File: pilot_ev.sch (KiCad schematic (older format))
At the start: 9 parts, among them Q201 AO3400A

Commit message: Add files via upload
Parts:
- removed TP201: TP_EV_PILOT, symbol Connector:TestPoint_Flag
- removed TP202: TP_EV_PILOT_ADC, symbol Connector:TestPoint_Flag
- added R206, R207: 200, Resistor_SMD:R_0402_1005Metric, symbol Device:R_Small_US
- added R208: 100, Resistor_SMD:R_0402_1005Metric, symbol Device:R_Small_US
- D201: footprint (none) -> Diode_SMD:D_SOD-123F
- Q201: footprint (none) -> Package_TO_SOT_SMD:SOT-23
- R201: value 2k74 -> 2k7; footprint (none) -> Resistor_SMD:R_0603_1608Metric
- R202, R204, R205: footprint (none) -> Resistor_SMD:R_0402_1005Metric
- R203: value 1k3 -> 1k2; footprint (none) -> Resistor_SMD:R_0402_1005Metric
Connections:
- wire segments 18 -> 22
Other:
- note added: "Total: 1k3"
- note added: "Total: 2k74"
- moved on the sheet: R203
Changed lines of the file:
@@
 U 1 1 5EEF9EDE
 P 3050 2600
-F 0 "R201" H 2982 2554 50  0000 R CNN
-F 1 "2k74" H 2982 2645 50  0000 R CNN
-F 2 "" H 3050 2600 50  0001 C CNN
+F 0 "R201" H 3300 2550 50  0000 R CNN
+F 1 "2k7" H 3300 2650 50  0000 R CNN
+F 2 "Resistor_SMD:R_0603_1608Metric" H 3050 2600 50  0001 C CNN
 F 3 "~" H 3050 2600 50  0001 C CNN
 	1    3050 2600
@@
 L Device:R_Small_US R203
 U 1 1 5EEFAC97
-P 3500 2600
-F 0 "R203" H 3432 2554 50  0000 R CNN
-F 1 "1k3" H 3432 2645 50  0000 R CNN
-F 2 "" H 3500 2600 50  0001 C CNN
-F 3 "~" H 3500 2600 50  0001 C CNN
-	1    3500 2600
+P 3500 2450
+F 0 "R203" H 3432 2404 50  0000 R CNN
+F 1 "1k2" H 3432 2495 50  0000 R CNN
+F 2 "Resistor_SMD:R_0402_1005Metric" H 3500 2450 50  0001 C CNN
+F 3 "~" H 3500 2450 50  0001 C CNN
+	1    3500 2450
 	-1   0    0    1
 $EndComp
@@
 F 0 "D201" H 2800 2093 50  0000 C CNN
 F 1 "SM4007PL" H 2800 2184 50  0000 C CNN
-F 2 "" V 2800 2300 50  0001 C CNN
+F 2 "Diode_SMD:D_SOD-123F" V 2800 2300 50  0001 C CNN
 F 3 "~" V 2800 2300 50  0001 C CNN
 	1    2800 2300
@@
 Wire Wire Line
 	2900 2300 3050 2300
-Wire Wire Line
-	3050 2300 3500 2300
-Wire Wire Line
-	3500 2300 3500 2500
 Connection ~ 3050 2300
 Wire Wire Line
@@
 F 0 "Q201" H 3605 3146 50  0000 L CNN
 F 1 "AO3400A" H 3605 3055 50  0000 L CNN
-F 2 "" H 3600 3200 50  0001 C CNN
+F 2 "Package_TO_SOT_SMD:SOT-23" H 3600 3200 50  0001 C CNN
 F 3 "~" H 3400 3100 50  0001 C CNN
 	1    3400 3100
-	1    0    0    -1
-$EndComp
-Wire Wire Line
-	3500 2900 3500 2700
-$Comp
-L power:GND #PWR0201
-U 1 1 5EEFDC0F
-P 3050 2750
-F 0 "#PWR0201" H 3050 2500 50  0001 C CNN
-F 1 "GND" H 3055 2577 50  0000 C CNN
-F 2 "" H 3050 2750 50  0001 C CNN
-F 3 "" H 3050 2750 50  0001 C CNN
-	1    3050 2750
 	1    0    0    -1
 $EndComp
@@
 F 0 "R204" H 4182 2554 50  0000 R CNN
 F 1 "47k" H 4182 2645 50  0000 R CNN
-F 2 "" H 4250 2600 50  0001 C CNN
+F 2 "Resistor_SMD:R_0402_1005Metric" H 4250 2600 50  0001 C CNN
 F 3 "~" H 4250 2600 50  0001 C CNN
 	1    4250 2600
@@
 F 0 "R205" H 4182 3054 50  0000 R CNN
 F 1 "18k" H 4182 3145 50  0000 R CNN
-F 2 "" H 4250 3100 50  0001 C CNN
+F 2 "Resistor_SMD:R_0402_1005Metric" H 4250 3100 50  0001 C CNN
 F 3 "~" H 4250 3100 50  0001 C CNN
 	1    4250 3100
@@
 $EndComp
 Wire Wire Line
-	3500 2300 4250 2300
-Wire Wire Line
 	4250 2300 4250 2500
-Connection ~ 3500 2300
 Wire Wire Line
 	4250 3000 4250 2850
@@
 F 0 "R202" H 2982 3204 50  0000 R CNN
 F 1 "10k" H 2982 3295 50  0000 R CNN
-F 2 "" H 3050 3250 50  0001 C CNN
+F 2 "Resistor_SMD:R_0402_1005Metric" H 3050 3250 50  0001 C CNN
 F 3 "~" H 3050 3250 50  0001 C CNN
 	1    3050 3250
@@
 $EndComp
 $Comp
-L Connector:TestPoint_Flag TP201
-U 1 1 5EF8CC23
-P 4250 2300
-F 0 "TP201" H 4510 2394 50  0000 L CNN
-F 1 "TP_EV_PILOT" H 4510 2303 50  0000 L CNN
-F 2 "" H 4450 2300 50  0001 C CNN
-F 3 "~" H 4450 2300 50  0001 C CNN
-	1    4250 2300
-	1    0    0    -1
-$EndComp
-Connection ~ 4250 2300
-$Comp
-L Connector:TestPoint_Flag TP202
-U 1 1 5EF8D1DC
-P 4250 2850
-F 0 "TP202" H 4550 3050 50  0000 L CNN
-F 1 "TP_EV_PILOT_ADC" H 4550 2950 50  0000 L CNN
-F 2 "" H 4450 2850 50  0001 C CNN
-F 3 "~" H 4450 2850 50  0001 C CNN
-	1    4250 2850
-	1    0    0    -1
-$EndComp
+L Device:R_Small_US R207
+U 1 1 5EF26A7F
+P 2950 2750
+F 0 "R207" V 2750 2850 50  0000 R CNN
+F 1 "200" V 2850 2850 50  0000 R CNN
+F 2 "Resistor_SMD:R_0402_1005Metric" H 2950 2750 50  0001 C CNN
+F 3 "~" H 2950 2750 50  0001 C CNN
+	1    2950 2750
+	0    -1   -1   0
+$EndComp
+$Comp
+L Device:R_Small_US R206
+U 1 1 5EF26C08
+P 2700 2750
+F 0 "R206" V 2500 2850 50  0000 R CNN
+F 1 "200" V 2600 2850 50  0000 R CNN
+F 2 "Resistor_SMD:R_0402_1005Metric" H 2700 2750 50  0001 C CNN
+F 3 "~" H 2700 2750 50  0001 C CNN
+	1    2700 2750
+	0    -1   -1   0
+$EndComp
+Wire Wire Line
+	2850 2750 2800 2750
+Wire Wire Line
+	2600 2750 2450 2750
+Wire Wire Line
+	2450 2750 2450 2800
+$Comp
+L power:GND #PWR0201
+U 1 1 5EF27EBA
+P 2450 2800
+F 0 "#PWR0201" H 2450 2550 50  0001 C CNN
+F 1 "GND" H 2455 2627 50  0000 C CNN
+F 2 "" H 2450 2800 50  0001 C CNN
+F 3 "" H 2450 2800 50  0001 C CNN
+	1    2450 2800
+	1    0    0    -1
+$EndComp
+Wire Notes Line
+	2550 2400 2550 3000
+Wire Notes Line
+	2550 3000 3150 3000
+Wire Notes Line
+	3150 3000 3150 2400
+Wire Notes Line
+	3150 2400 2550 2400
+Text Notes 2550 2500 0    50   ~ 0
+Total: 2k74
+Wire Wire Line
+	3050 2300 3500 2300
+$Comp
+L Device:R_Small_US R208
+U 1 1 5EF2A29D
+P 3500 2700
+F 0 "R208" H 3432 2654 50  0000 R CNN
+F 1 "100" H 3432 2745 50  0000 R CNN
+F 2 "Resistor_SMD:R_0402_1005Metric" H 3500 2700 50  0001 C CNN
+F 3 "~" H 3500 2700 50  0001 C CNN
+	1    3500 2700
+	-1   0    0    1
+$EndComp
+Wire Wire Line
+	3500 2300 3500 2350
+Connection ~ 3500 2300
+Wire Wire Line
+	3500 2300 4250 2300
+Wire Wire Line
+	3500 2550 3500 2600
+Wire Wire Line
+	3500 2800 3500 2900
+Wire Notes Line
+	3400 2350 3400 2850
+Wire Notes Line
+	3400 2850 3800 2850
+Wire Notes Line
+	3800 2850 3800 2350
+Wire Notes Line
+	3800 2350 3400 2350
+Text Notes 3400 2800 1    50   ~ 0
+Total: 1k3
 $EndSCHEMATC

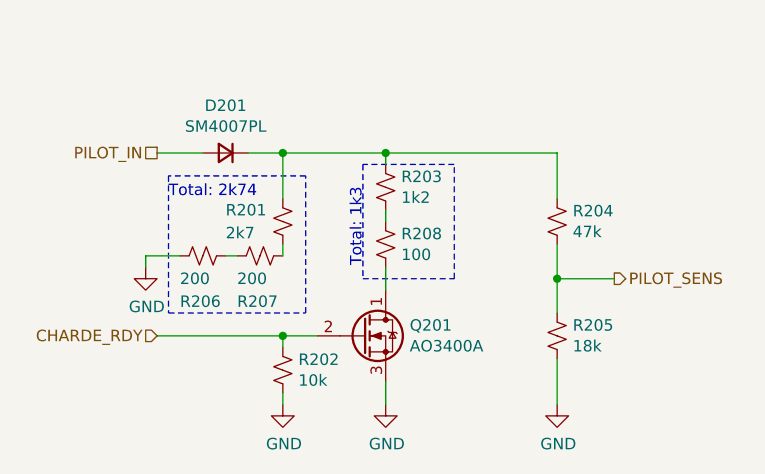
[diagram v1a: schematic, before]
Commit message: Submited for production & smt assembly
v0.01
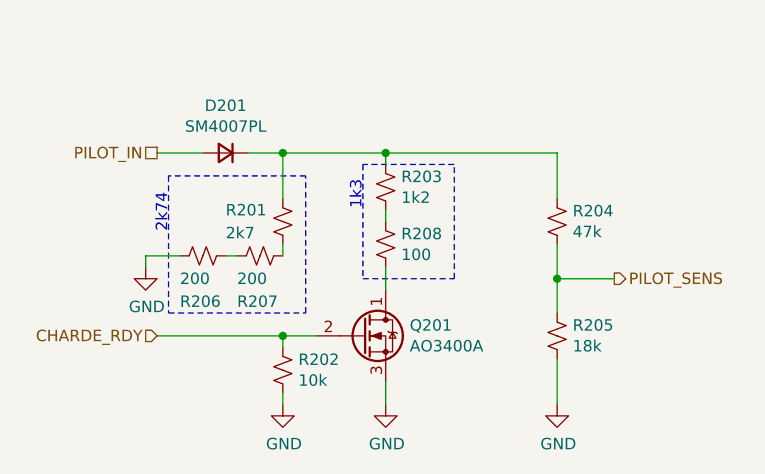
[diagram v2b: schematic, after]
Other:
- note added: "1k3"
- note added: "2k74"
- note removed: "Total: 1k3"
- note removed: "Total: 2k74"
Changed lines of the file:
@@
 Wire Notes Line
 	3150 2400 2550 2400
-Text Notes 2550 2500 0    50   ~ 0
-Total: 2k74
+Text Notes 2550 2650 1    50   ~ 0
+2k74
 Wire Wire Line
 	3050 2300 3500 2300
@@
 Wire Notes Line
 	3800 2350 3400 2350
-Text Notes 3400 2800 1    50   ~ 0
-Total: 1k3
+Text Notes 3400 2550 1    50   ~ 0
+1k3
 $EndSCHEMATC
